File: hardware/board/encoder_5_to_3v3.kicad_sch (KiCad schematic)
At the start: 7 parts, among them J7 Conn_01x04_Female, U15 74LVCH2T45DC

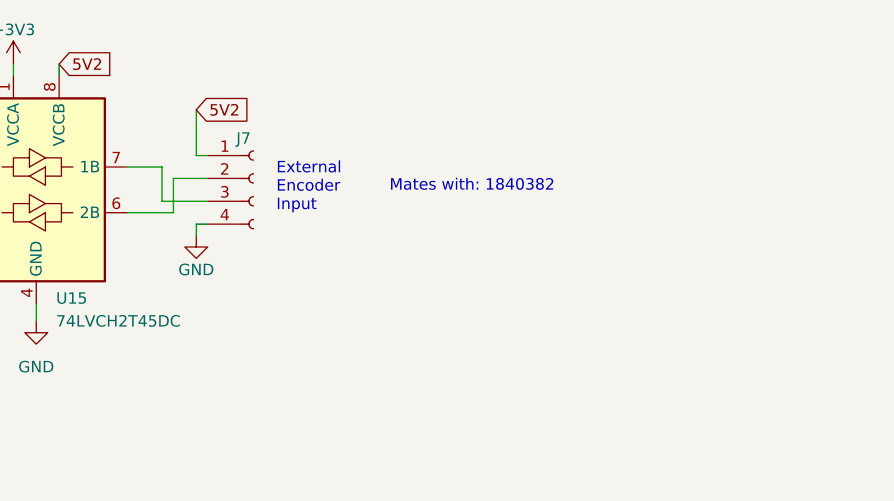
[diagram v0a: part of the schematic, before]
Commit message: add tvs diodes to inputs
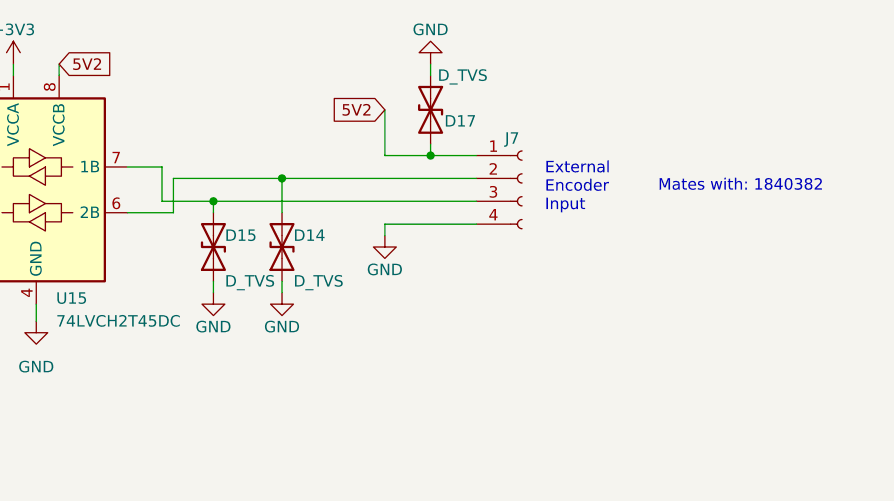
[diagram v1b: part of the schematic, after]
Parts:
- added D14, D15, D17: D_TVS, Diode_SMD:D_SOD-882D, symbol Device:D_TVS
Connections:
- net 5V2: now also D17.2 (A2)
- net GND: now also D14.1 (A1), D15.1 (A1), D17.1 (A1)
- net at J7.2 (Pin_2), U15.6 (2B): now also D14.2 (A2)
- net at J7.3 (Pin_3), U15.7 (1B): now also D15.2 (A2)
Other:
- moved on the sheet: J7
